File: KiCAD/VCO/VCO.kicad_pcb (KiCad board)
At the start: 2 copper layers, 50 x 100 mm, 42 parts, among them J1 CV IN 1, J2 CV IN 2, J3 PWM, J4 SAW OUT, J5 PULSE OUT, J6 Conn_01x03_Pin, J7 Conn_01x03_Pin, Q1 NPN, T1 PNP, T2 NPN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

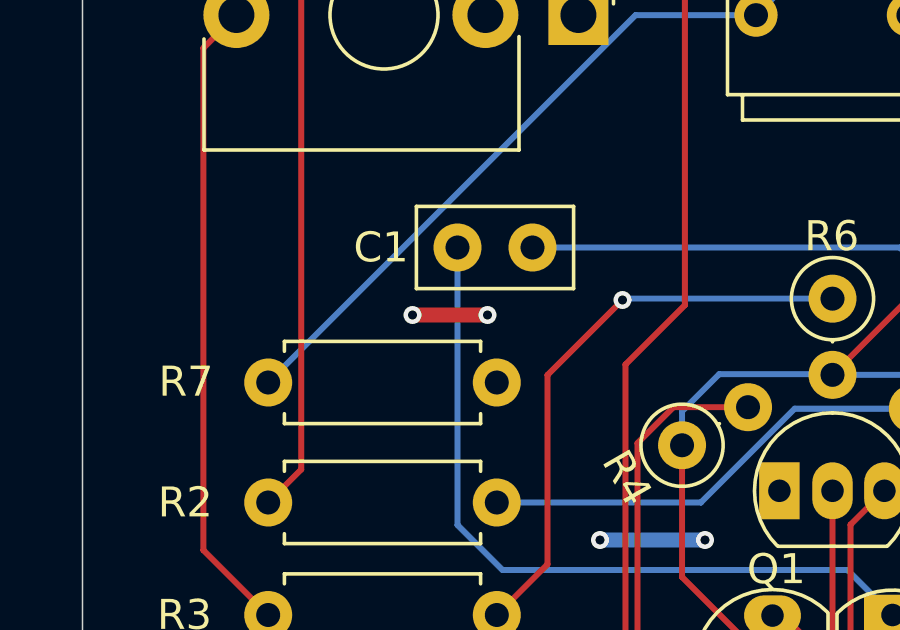
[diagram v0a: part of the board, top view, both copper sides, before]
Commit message: remove unnecessary tracks
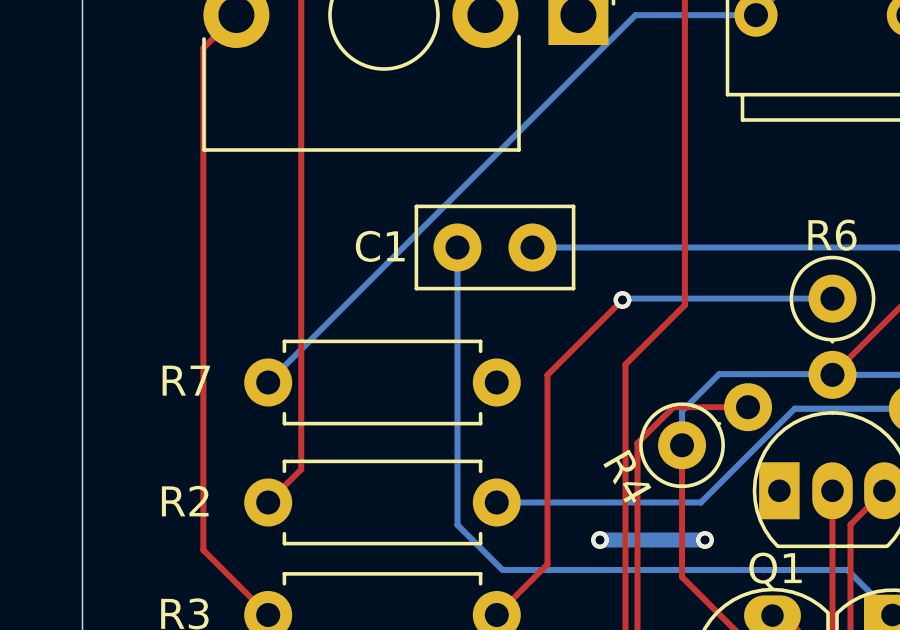
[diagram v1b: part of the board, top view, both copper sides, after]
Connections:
- J6 pad 2: VDD -> GND
- J7 pad 2: VDD -> GND
- Q1 pad 1: VDD -> GND
- R10 pad 1: VDD -> GND
- R13 pad 1: VDD -> GND
- RV3 pad 1: VDD -> GND
- U1 pad 14: VDD -> GND
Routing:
- net VDD: track 9.00 -> 3.00 mm, vias 6 -> 2
- net GND: track 0.00 -> 3.50 mm, vias 0 -> 2
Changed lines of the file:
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@@
 			(layers "*.Cu" "*.Mask")
 			(remove_unused_layers no)
-			(net 17 "VDD")
+			(net 9 "GND")
 			(pinfunction "1")
 			(pintype "passive")
@@
 			(layers "*.Cu" "*.Mask")
 			(remove_unused_layers no)
-			(net 17 "VDD")
+			(net 9 "GND")
 			(pinfunction "C")
 			(pintype "open_collector")
@@
 			(layers "*.Cu" "*.Mask")
 			(remove_unused_layers no)
-			(net 17 "VDD")
+			(net 9 "GND")
 			(pinfunction "Pin_2")
 			(pintype "passive")
@@
 			(layers "*.Cu" "*.Mask")
 			(remove_unused_layers no)
-			(net 17 "VDD")
+			(net 9 "GND")
 			(pinfunction "VDD")
 			(pintype "power_in")
@@
 			(layers "*.Cu" "*.Mask")
 			(remove_unused_layers no)
-			(net 17 "VDD")
+			(net 9 "GND")
 			(pintype "passive")
 		)
@@
 			(layers "*.Cu" "*.Mask")
 			(remove_unused_layers no)
-			(net 17 "VDD")
+			(net 9 "GND")
 			(pintype "passive")
 		)
@@
 			(layers "*.Cu" "*.Mask")
 			(remove_unused_layers no)
-			(net 17 "VDD")
+			(net 9 "GND")
 			(pinfunction "Pin_2")
 			(pintype "passive")
@@
 		(net 7)
 	)
+	(via
+		(at 70.75 95)
+		(size 0.6)
+		(drill 0.3)
+		(layers "F.Cu" "B.Cu")
+		(free yes)
+		(net 9)
+	)
+	(via
+		(at 67.25 95)
+		(size 0.6)
+		(drill 0.3)
+		(layers "F.Cu" "B.Cu")
+		(free yes)
+		(net 9)
+	)
+	(segment
+		(start 67.25 95)
+		(end 70.75 95)
+		(width 0.5)
+		(layer "B.Cu")
+		(net 9)
+	)
 	(segment
 		(start 57.291 64.711)
@@
 		(net 17)
 	)
-	(segment
-		(start 61 87.5)
-		(end 63.5 87.5)
-		(width 0.5)
-		(layer "F.Cu")
-		(net 17)
-	)
-	(via
-		(at 61 87.5)
-		(size 0.6)
-		(drill 0.3)
-		(layers "F.Cu" "B.Cu")
-		(free yes)
-		(net 17)
-	)
 	(via
 		(at 74.75 114.25)
@@
 	)
 	(via
-		(at 70.75 95)
-		(size 0.6)
-		(drill 0.3)
-		(layers "F.Cu" "B.Cu")
-		(net 17)
-	)
-	(via
-		(at 63.5 87.5)
-		(size 0.6)
-		(drill 0.3)
-		(layers "F.Cu" "B.Cu")
-		(net 17)
-	)
-	(via
-		(at 67.25 95)
-		(size 0.6)
-		(drill 0.3)
-		(layers "F.Cu" "B.Cu")
-		(free yes)
-		(net 17)
-	)
-	(via
 		(at 74.75 117.25)
 		(size 0.6)
@@
 		(net 17)
 	)
-	(segment
-		(start 67.25 95)
-		(end 70.75 95)
-		(width 0.5)
-		(layer "B.Cu")
-		(net 17)
-	)

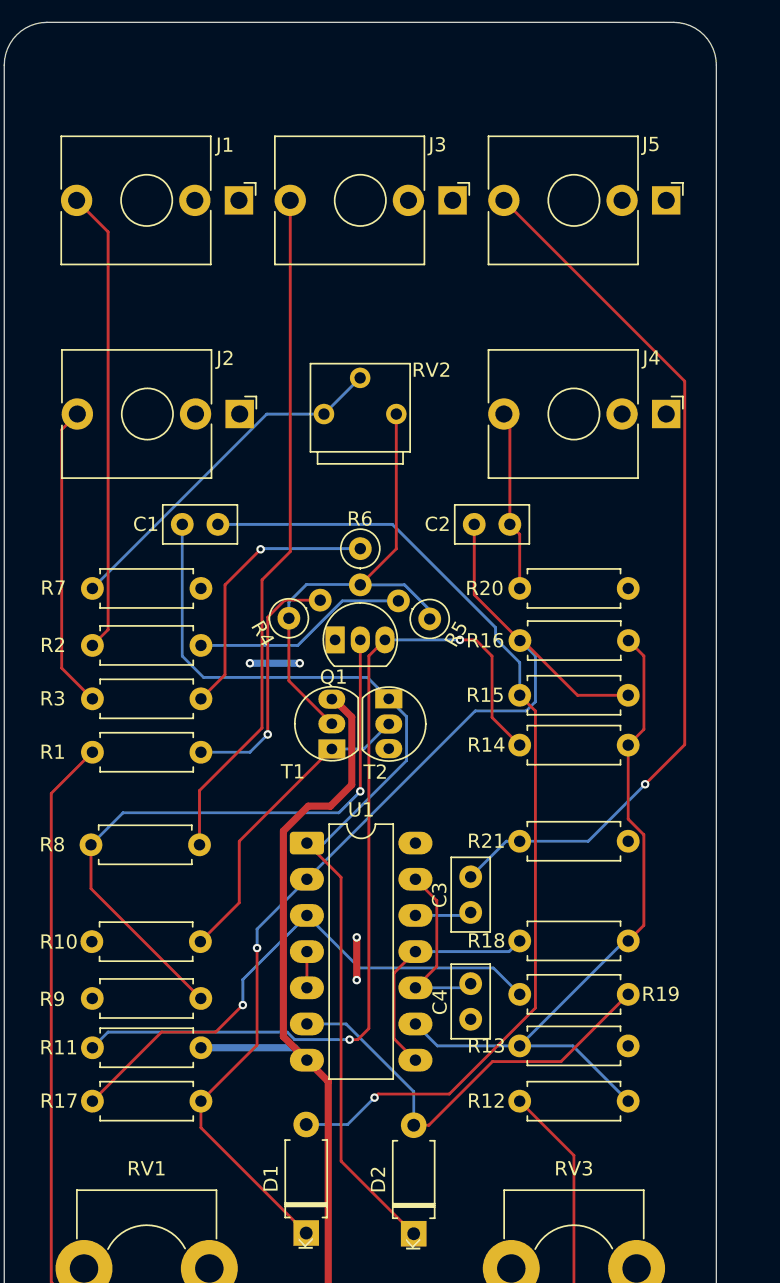
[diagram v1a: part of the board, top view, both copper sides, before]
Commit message: Rearrange text and add labels
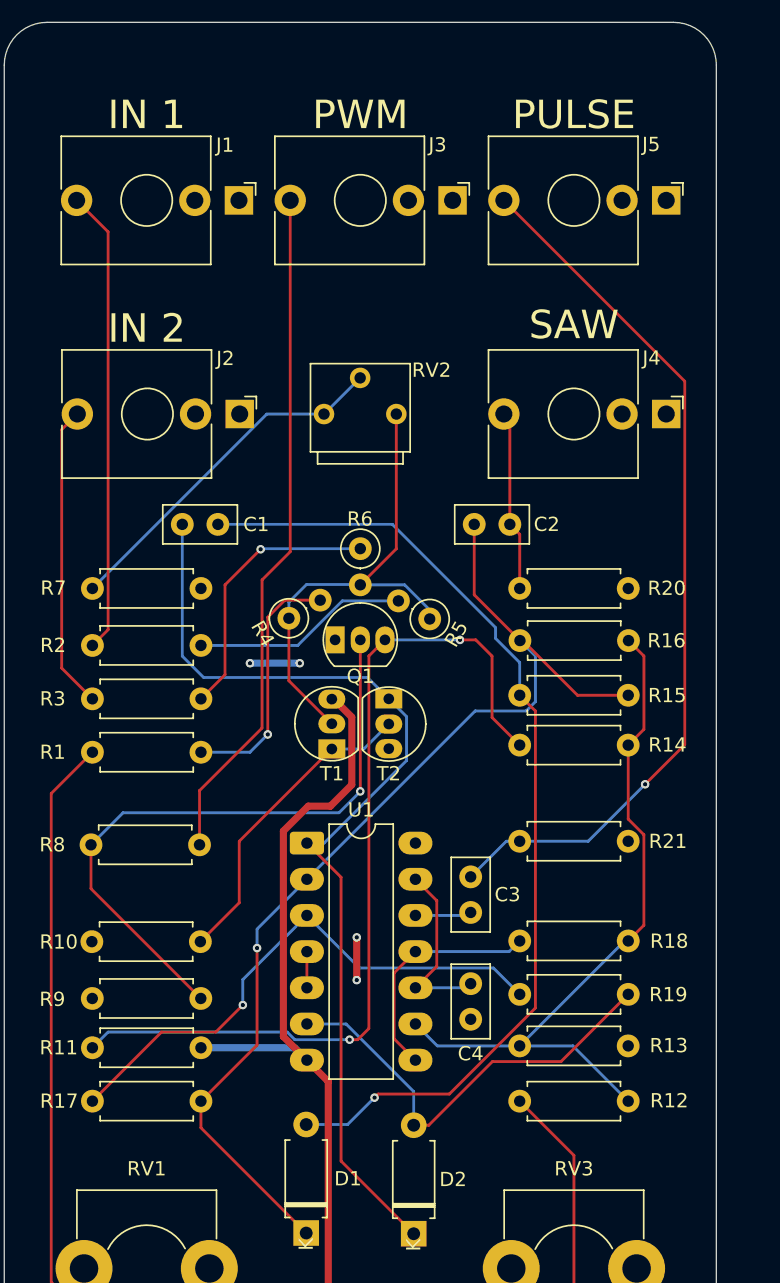
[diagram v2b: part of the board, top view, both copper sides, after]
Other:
- board text added: "IN 1"
- board text added: "IN 2"
- board text added: "PULSE"
- board text added: "PWM"
- board text added: "SAW"
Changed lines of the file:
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@@
 		(tags "to-92 sc-43 sc-43a sot54 PA33 transistor")
 		(property "Reference" "Q1"
-			(at -0.605 2.615 0)
+			(at 1.28 2.56 0)
 			(layer "F.SilkS")
 			(effects
@@
 		(tags "Resistor Axial_DIN0207 series Axial Horizontal pin pitch 7.62mm 0.25W = 1/4W length 6.3mm diameter 2.5mm")
 		(property "Reference" "R21"
-			(at -2.34 0 0)
+			(at 10.41 0.01 0)
 			(layer "F.SilkS")
 			(effects
@@
 		(tags "C Disc series Radial pin pitch 2.50mm  diameter 5mm width 2.5mm Capacitor")
 		(property "Reference" "C3"
-			(at 1.225 -2.175 90)
+			(at 1.25 2.59 180)
 			(layer "F.SilkS")
 			(effects
@@
 		(tags "Resistor Axial_DIN0207 series Axial Horizontal pin pitch 7.62mm 0.25W = 1/4W length 6.3mm diameter 2.5mm")
 		(property "Reference" "R20"
-			(at -2.468333 0 0)
+			(at 10.326667 -0.01 0)
 			(layer "F.SilkS")
 			(effects
@@
 		(tags "Resistor Axial_DIN0207 series Axial Horizontal pin pitch 7.62mm 0.25W = 1/4W length 6.3mm diameter 2.5mm")
 		(property "Reference" "R12"
-			(at -2.34 0 0)
+			(at 10.5 -0.03 0)
 			(layer "F.SilkS")
 			(effects
@@
 		(tags "C Disc series Radial pin pitch 2.50mm  diameter 5mm width 2.5mm Capacitor")
 		(property "Reference" "C1"
-			(at -2.55 0 0)
+			(at 5.19 0.01 0)
 			(layer "F.SilkS")
 			(effects
@@
 		(tags "Resistor Axial_DIN0207 series Axial Horizontal pin pitch 7.62mm 0.25W = 1/4W length 6.3mm diameter 2.5mm")
 		(property "Reference" "R16"
-			(at -2.435 0.015 0)
+			(at 10.29 0.015 0)
 			(layer "F.SilkS")
 			(effects
@@
 		(tags "Diode A-405 series Axial Horizontal pin pitch 7.62mm  length 5.2mm diameter 2.7mm")
 		(property "Reference" "D1"
-			(at 3.81 -2.47 90)
+			(at 3.81 2.93 180)
 			(layer "F.SilkS")
 			(effects
@@
 		(tags "Resistor Axial_DIN0207 series Axial Horizontal pin pitch 7.62mm 0.25W = 1/4W length 6.3mm diameter 2.5mm")
 		(property "Reference" "R19"
-			(at 9.906667 0 0)
+			(at 10.436667 0.02 0)
 			(layer "F.SilkS")
 			(effects
@@
 		(tags "C Disc series Radial pin pitch 2.50mm  diameter 5mm width 2.5mm Capacitor")
 		(property "Reference" "C4"
-			(at 1.2 -2.15 90)
+			(at -2.42 0 180)
 			(layer "F.SilkS")
 			(effects
@@
 		(tags "Resistor Axial_DIN0207 series Axial Horizontal pin pitch 7.62mm 0.25W = 1/4W length 6.3mm diameter 2.5mm")
 		(property "Reference" "R13"
-			(at 9.96 -0.005 0)
+			(at -2.85 0.02 0)
 			(layer "F.SilkS")
 			(effects
@@
 		(tags "C Disc series Radial pin pitch 2.50mm  diameter 5mm width 2.5mm Capacitor")
 		(property "Reference" "C2"
-			(at -2.575 0 0)
+			(at 5.09 0 0)
 			(layer "F.SilkS")
 			(effects
@@
 		(tags "to-92 sc-43 sc-43a sot54 PA33 transistor")
 		(property "Reference" "T2"
-			(at 4.65 0.925 180)
+			(at 4.76 0 180)
 			(layer "F.SilkS")
 			(effects
@@
 		(tags "to-92 sc-43 sc-43a sot54 PA33 transistor")
 		(property "Reference" "T1"
-			(at -2.105 -2.725 180)
+			(at -2.24 0.01 180)
 			(layer "F.SilkS")
 			(effects
@@
 		(tags "Diode A-405 series Axial Horizontal pin pitch 7.62mm  length 5.2mm diameter 2.7mm")
 		(property "Reference" "D2"
-			(at 3.81 -2.47 90)
+			(at 3.81 2.76 180)
 			(layer "F.SilkS")
 			(effects
@@
 		(tags "Resistor Axial_DIN0207 series Axial Horizontal pin pitch 7.62mm 0.25W = 1/4W length 6.3mm diameter 2.5mm")
 		(property "Reference" "R14"
-			(at -2.34 0 0)
+			(at 10.38 -0.01 0)
 			(layer "F.SilkS")
 			(effects
@@
 		(tags "Resistor Axial_DIN0207 series Axial Horizontal pin pitch 7.62mm 0.25W = 1/4W length 6.3mm diameter 2.5mm")
 		(property "Reference" "R18"
-			(at 9.963333 0 180)
+			(at -2.876667 -0.02 180)
 			(layer "F.SilkS")
 			(effects
@@
 		(tags "Resistor Axial_DIN0207 series Axial Horizontal pin pitch 7.62mm 0.25W = 1/4W length 6.3mm diameter 2.5mm")
 		(property "Reference" "R15"
-			(at -2.418333 0 0)
+			(at 10.356667 0.02 0)
 			(layer "F.SilkS")
 			(effects
@@
 			)
 		)
+	)
+	(gr_text "IN 2"
+		(at 60 71.5 0)
+		(layer "F.SilkS")
+		(effects
+			(font
+				(size 2 2)
+				(thickness 0.3)
+			)
+		)
+	)
+	(gr_text "PWM"
+		(at 75 56.5 0)
+		(layer "F.SilkS")
+		(effects
+			(font
+				(size 2 2)
+				(thickness 0.3)
+			)
+		)
+	)
+	(gr_text "SAW"
+		(at 90 71.25 0)
+		(layer "F.SilkS")
+		(effects
+			(font
+				(size 2 2)
+				(thickness 0.3)
+			)
+		)
+	)
+	(gr_text "PULSE"
+		(at 90 56.5 0)
+		(layer "F.SilkS")
+		(effects
+			(font
+				(size 2 2)
+				(thickness 0.3)
+			)
+		)
+	)
+	(gr_text "IN 1"
+		(at 60 56.5 0)
+		(layer "F.SilkS")
+		(effects
+			(font
+				(size 2 2)
+				(thickness 0.3)
+			)
+		)

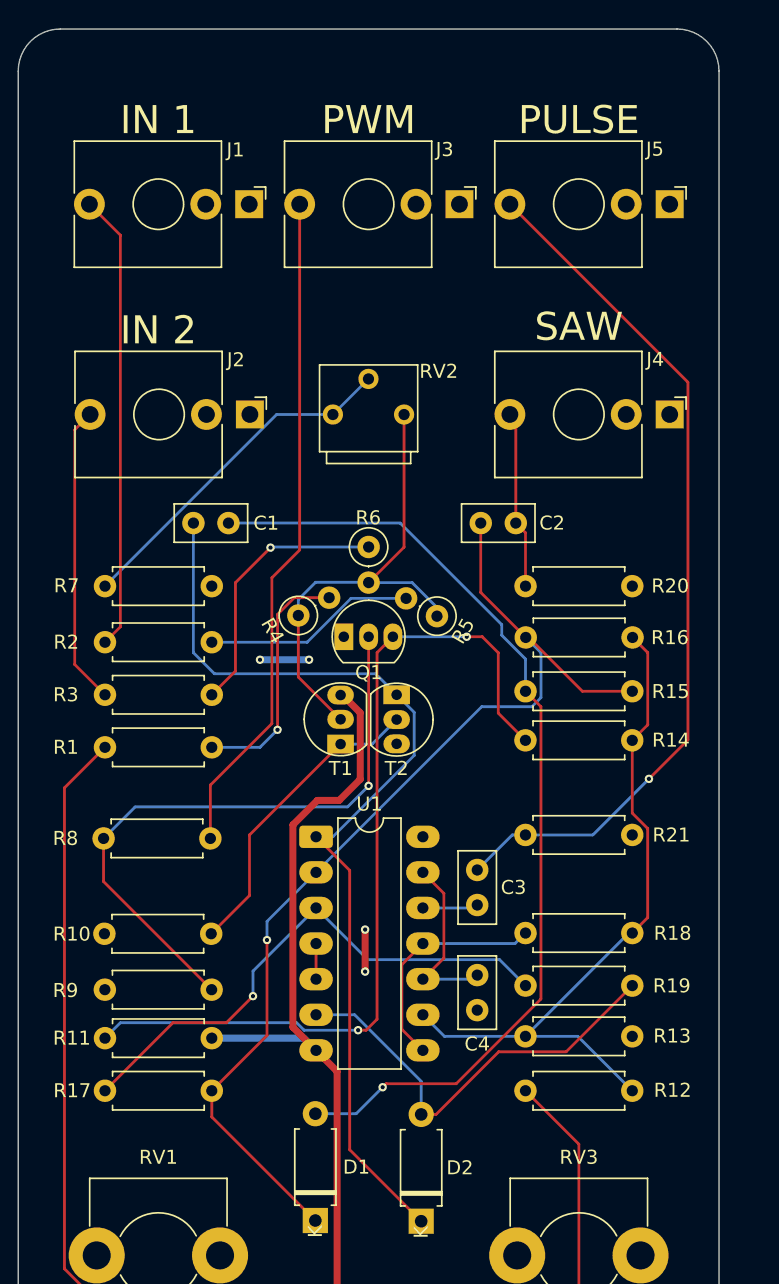
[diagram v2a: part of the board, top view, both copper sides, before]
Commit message: Adjustments to labels
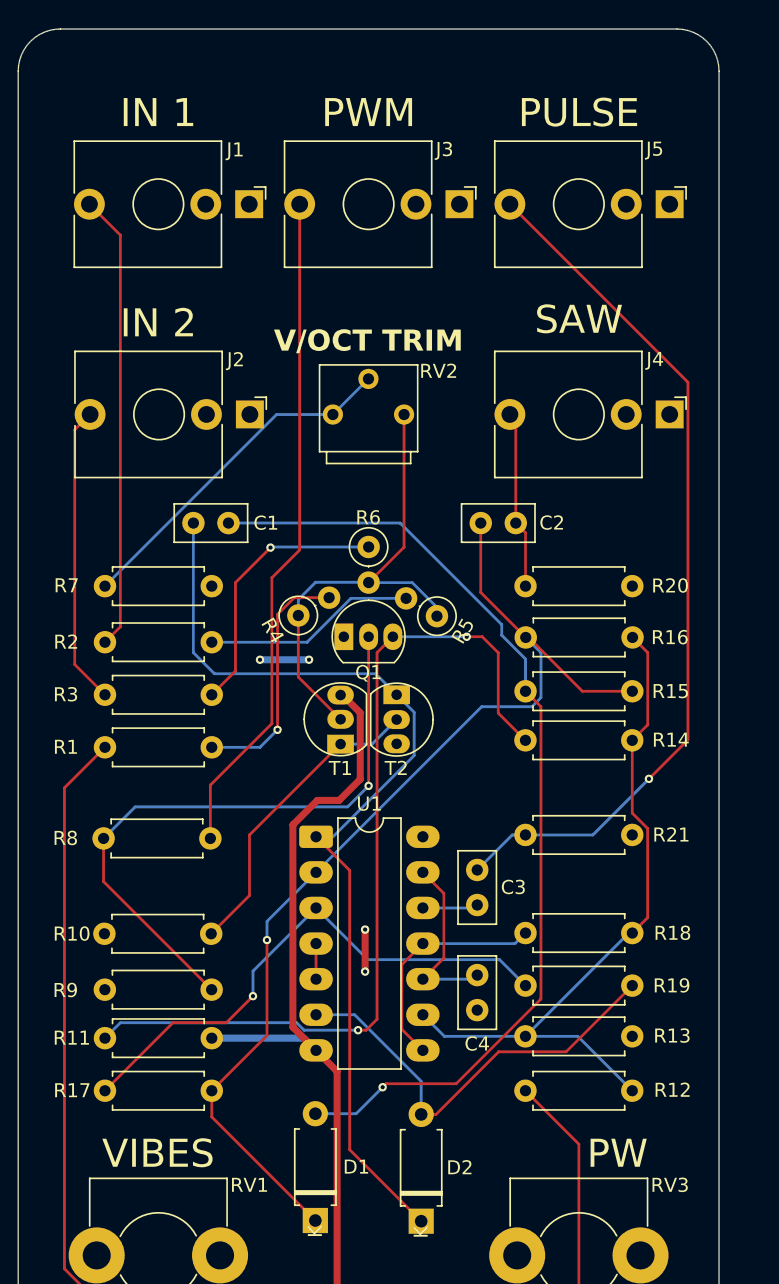
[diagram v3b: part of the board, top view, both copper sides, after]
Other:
- board text added: "PW"
- board text added: "V/OCT TRIM"
- board text added: "VIBES"
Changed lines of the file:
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@@
 		(tags "Potentiometer horizontal  Omeg PC16PU  Omeg PC16PU  Omeg PC16PU  Vishay/Spectrol 248GJ/249GJ Single  Vishay/Spectrol 248GJ/249GJ Single  Vishay/Spectrol 248GJ/249GJ Single  Vishay/Spectrol 248GH/249GH Single  Vishay/Spectrol 148/149 Single  Vishay/Spectrol 148/149 Single  Vishay/Spectrol 148/149 Single  Vishay/Spectrol 148A/149A Single with mounting plates  Vishay/Spectrol 148/149 Double  Vishay/Spectrol 148A/149A Double with mounting plates  Piher PC-16 Single  Piher PC-16 Single  Piher PC-16 Single  Piher PC-16SV Single  Piher PC-16 Double  Piher PC-16 Triple  Piher T16H Single  Piher T16L Single  Piher T16H Double  Alps RK163 Single  Alps RK163 Double  Alps RK097 Single  Alps RK097 Double  Bourns PTV09A-2 Single with mounting sleve Single  Bourns PTV09A-1 with mounting sleve Single  Bourns PRS11S Single  Alps RK09K Single with mounting sleve Single  Alps RK09K with mounting sleve Single")
 		(property "Reference" "RV3"
-			(at 0 -7 0)
+			(at 6.5 -5 0)
 			(layer "F.SilkS")
 			(effects
@@
 		(tags "Potentiometer horizontal  Omeg PC16PU  Omeg PC16PU  Omeg PC16PU  Vishay/Spectrol 248GJ/249GJ Single  Vishay/Spectrol 248GJ/249GJ Single  Vishay/Spectrol 248GJ/249GJ Single  Vishay/Spectrol 248GH/249GH Single  Vishay/Spectrol 148/149 Single  Vishay/Spectrol 148/149 Single  Vishay/Spectrol 148/149 Single  Vishay/Spectrol 148A/149A Single with mounting plates  Vishay/Spectrol 148/149 Double  Vishay/Spectrol 148A/149A Double with mounting plates  Piher PC-16 Single  Piher PC-16 Single  Piher PC-16 Single  Piher PC-16SV Single  Piher PC-16 Double  Piher PC-16 Triple  Piher T16H Single  Piher T16L Single  Piher T16H Double  Alps RK163 Single  Alps RK163 Double  Alps RK097 Single  Alps RK097 Double  Bourns PTV09A-2 Single with mounting sleve Single  Bourns PTV09A-1 with mounting sleve Single  Bourns PRS11S Single  Alps RK09K Single with mounting sleve Single  Alps RK09K with mounting sleve Single")
 		(property "Reference" "RV1"
-			(at 0 -7 0)
+			(at 6.5 -5 0)
 			(layer "F.SilkS")
 			(effects
@@
 	)
 	(gr_text "IN 2"
-		(at 60 71.5 0)
+		(at 60 71 0)
 		(layer "F.SilkS")
 		(effects
@@
 	)
 	(gr_text "PWM"
-		(at 75 56.5 0)
+		(at 75 56 0)
 		(layer "F.SilkS")
 		(effects
@@
 	)
 	(gr_text "SAW"
-		(at 90 71.25 0)
+		(at 90 70.75 0)
+		(layer "F.SilkS")
+		(effects
+			(font
+				(size 2 2)
+				(thickness 0.3)
+			)
+		)
+	)
+	(gr_text "VIBES"
+		(at 60 130.25 0)
 		(layer "F.SilkS")
 		(effects
@@
 	)
 	(gr_text "PULSE"
-		(at 90 56.5 0)
+		(at 90 56 0)
 		(layer "F.SilkS")
 		(effects
@@
 	)
 	(gr_text "IN 1"
-		(at 60 56.5 0)
+		(at 60 56 0)
+		(layer "F.SilkS")
+		(effects
+			(font
+				(size 2 2)
+				(thickness 0.3)
+			)
+		)
+	)
+	(gr_text "PW"
+		(at 92.75 130.25 0)
 		(layer "F.SilkS")
 		(effects
@@
 			)
 		)
+	)
+	(gr_text "V/OCT TRIM"
+		(at 75 72.25 0)
+		(layer "F.SilkS")
+		(effects
+			(font
+				(size 1.5 1.5)
+				(thickness 0.25)
+				(bold yes)
+			)
+		)
